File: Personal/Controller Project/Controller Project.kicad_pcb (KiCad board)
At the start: 2 copper layers, 167.6 x 144.8 mm, 54 parts, among them IC1 SS49E, IC2 SS49E, SW1 SW_Push, SW10 SW_Push, SW11 SW_Push, SW12 SW_Push, SW2 SW_Push, SW3 SW_Push, SW4 SW_Push, SW5 SW_Push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

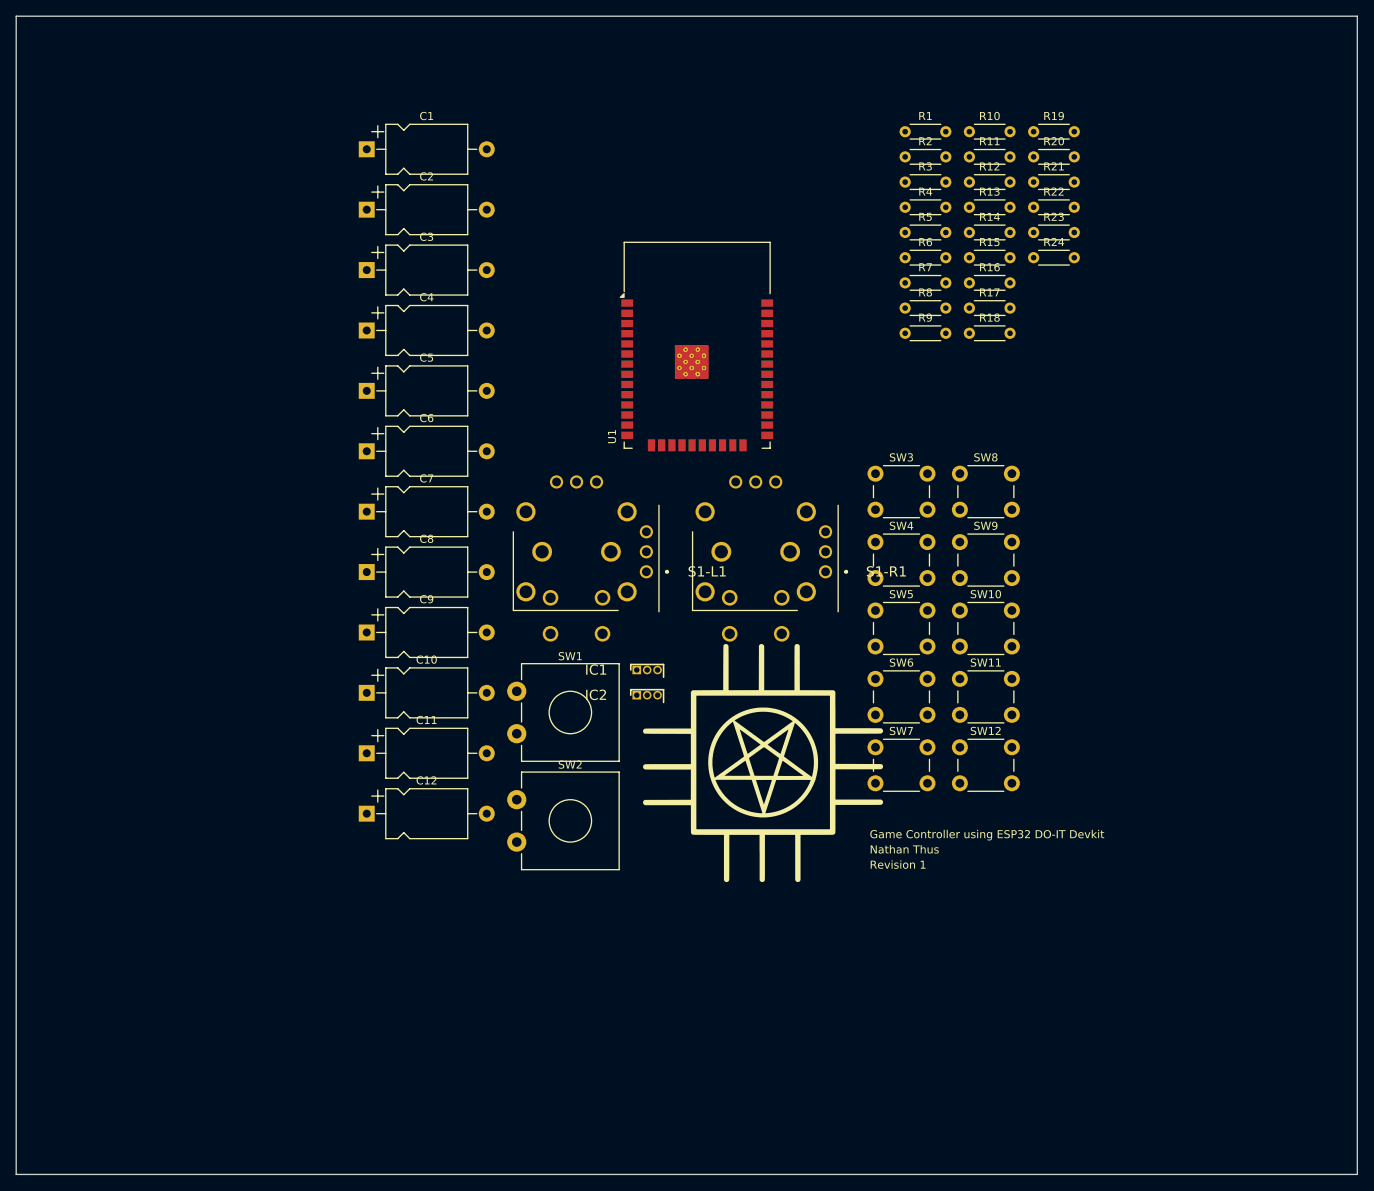
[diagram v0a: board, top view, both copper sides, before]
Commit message: 🍱 Update Trace Design for PCB
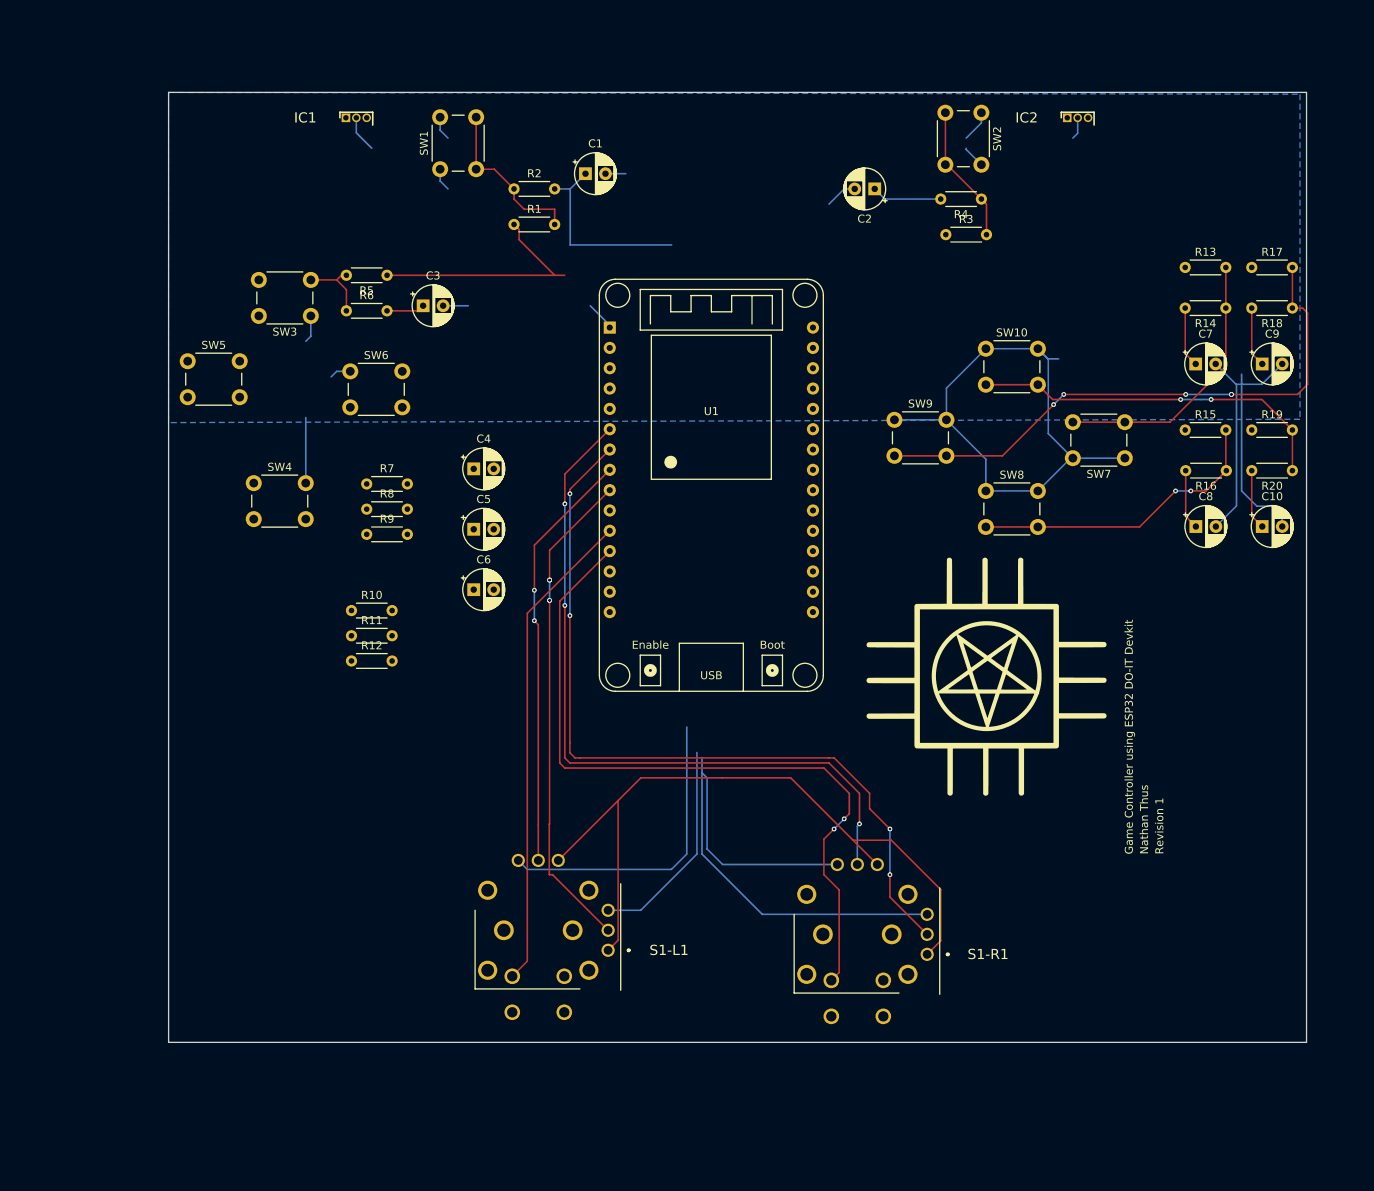
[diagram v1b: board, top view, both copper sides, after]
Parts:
- removed C11, C12: 10nF, Capacitor_THT:CP_Axial_L10.0mm_D6.0mm_P15.00mm_Horizontal
- removed R21, R22, R23, R24: 1k, Resistor_THT:R_Axial_DIN0204_L3.6mm_D1.6mm_P5.08mm_Horizontal
- removed SW11, SW12: SW_Push, Button_Switch_THT:SW_PUSH_6mm
- C1, C10, C2, C3, C4, C5, C6, C7, C8, C9: footprint Capacitor_THT:CP_Axial_L10.0mm_D6.0mm_P15.00mm_Horizontal -> Capacitor_THT:CP_Radial_D5.0mm_P2.50mm
- SW1, SW2: footprint Button_Switch_THT:SW_CW_GPTS203211B -> Button_Switch_THT:SW_PUSH_6mm
- U1: footprint RF_Module:ESP32-WROOM-32 -> esp32_devkit_v1_doit:esp32_devkit_v1_doit
- moved C9 116.9 mm to (214.2, 62.5)
- moved C10 113.9 mm to (214.2, 82.8)
- moved C7 105.2 mm to (205.9, 62.5)
- moved C8 103.8 mm to (205.9, 82.8)
- moved SW2 103.7 mm to (179.1, 31.1), turned to -90 degrees
- moved R10 97.7 mm to (100.3, 93.3)
- moved R11 97.7 mm to (100.3, 96.5)
- moved R12 97.7 mm to (100.3, 99.6)
- moved SW5 91.4 mm to (79.9, 62.2)
- moved IC2 90.0 mm to (189.8, 31.8)
- moved SW4 78.1 mm to (88.1, 77.4)
- moved IC1 78.0 mm to (99.6, 31.8)
- moved SW6 76.1 mm to (100.2, 63.4)
- moved SW3 73.3 mm to (95.2, 56.5), turned to 180 degrees
- moved R7 71.8 mm to (102.2, 77.5)
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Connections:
- S1-L1 pad MH1: GND -> unconnected-(S1-L1-PadMH1)
- S1-L1 pad MH2: GND -> unconnected-(S1-L1-PadMH2)
- S1-L1 pad MH3: GND -> unconnected-(S1-L1-PadMH3)
- S1-L1 pad MH4: GND -> unconnected-(S1-L1-PadMH4)
- S1-L1 pad MH5: GND -> unconnected-(S1-L1-PadMH5)
- S1-L1 pad MH6: GND -> unconnected-(S1-L1-PadMH6)
- S1-R1 pad MH1: GND -> unconnected-(S1-R1-PadMH1)
- S1-R1 pad MH2: GND -> unconnected-(S1-R1-PadMH2)
- S1-R1 pad MH3: GND -> unconnected-(S1-R1-PadMH3)
- S1-R1 pad MH4: GND -> unconnected-(S1-R1-PadMH4)
- S1-R1 pad MH5: GND -> unconnected-(S1-R1-PadMH5)
- S1-R1 pad MH6: GND -> unconnected-(S1-R1-PadMH6)
- U1 pad 13: unconnected-(U1-IO14-Pad13) -> /BTN_LB
- U1 pad 23: unconnected-(U1-IO15-Pad23) -> /BTN_RB
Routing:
- net GND: track 0.00 -> 307.1 mm
- net +3V3: track 0.00 -> 120.9 mm
- net /S1_R1_Y: track 0.00 -> 100.1 mm, vias 0 -> 4
- net /S1_R1_SW: track 0.00 -> 92.7 mm, vias 0 -> 2
- net /S1_R1_X: track 0.00 -> 91.1 mm, vias 0 -> 3
- net Net-(R17-Pad2): track 0.00 -> 71.5 mm, vias 0 -> 5
- net /S1_L1_Y: track 0.00 -> 61.4 mm, vias 0 -> 4
- net /S1_L1_SW: track 0.00 -> 60.7 mm
- net /S1_L1_X: track 0.00 -> 52.9 mm, vias 0 -> 2
- net Net-(R19-Pad2): track 0.00 -> 45.7 mm, vias 0 -> 2
- net Net-(R15-Pad2): track 0.00 -> 38.1 mm, vias 0 -> 2
- net Net-(R13-Pad2): track 0.00 -> 34.4 mm
- net /BTN_RB: track 0.00 -> 24.3 mm
- net Net-(R1-Pad2): track 0.00 -> 21.0 mm
- net Net-(R3-Pad2): track 0.00 -> 17.6 mm
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- added copper zone on B.Cu, net GND
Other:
- board size 167.6 x 144.8 mm -> 142.2 x 118.7 mm

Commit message: 📝 Add the last documentation regarding the project
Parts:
- moved R5 45.8 mm to (79.4, 89.5), turned to 0 degrees
- moved C3 42.6 mm to (88.9, 92.7)
- moved R6 41.6 mm to (84.5, 94.6), turned to 180 degrees
- moved C6 29.3 mm to (88.9, 102.9)
- moved C5 23.4 mm to (102.9, 102.9)
- moved R11 21.3 mm to (79.4, 100.4)
- moved C4 21.3 mm to (102.9, 92.7)
- moved R9 18.2 mm to (94.6, 100.4)
- moved R12 16.9 mm to (84.5, 105.6), turned to 180 degrees
- moved R7 14.2 mm to (94.6, 89.5)
- moved R8 14.2 mm to (99.7, 94.6), turned to 180 degrees
- moved R10 13.4 mm to (94.6, 105.4)
- moved SW4 6.33 mm to (88.8, 71.1)
- moved SW6 3.14 mm to (97.6, 61.6)
- moved SW5 0.58 mm to (79.9, 61.6)
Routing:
- net +3V3: track 120.9 -> 423.6 mm, vias 0 -> 13
- net +3.3V: track 0.00 -> 268.4 mm, vias 0 -> 3
- net GND: track 307.1 -> 502.3 mm
- net /IC_RT: track 0.00 -> 113.1 mm, vias 0 -> 9
- net /BTN_Y: track 7.55 -> 93.5 mm
- net /BTN_DPAD_RIGHT: track 0.00 -> 79.9 mm, vias 0 -> 3
- net Net-(R10-Pad2): track 0.00 -> 69.3 mm
- net /BTN_X: track 7.53 -> 67.6 mm
- net Net-(R11-Pad1): track 0.00 -> 58.7 mm
- net /BTN_A: track 7.53 -> 55.2 mm, vias 0 -> 2
- net Net-(R5-Pad2): track 9.05 -> 46.9 mm, vias 0 -> 3
- net /BTN_RB: track 24.3 -> 56.0 mm, vias 0 -> 5
- net /BTN_DPAD_LEFT: track 0.00 -> 21.3 mm, vias 0 -> 2
- net Net-(R7-Pad2): track 0.00 -> 20.8 mm
- net /BTN_DPAD_DOWN: track 0.00 -> 9.08 mm
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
